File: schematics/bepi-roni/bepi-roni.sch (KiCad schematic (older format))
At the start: 45 parts, among them J1 Conn_01x02, J2 Conn_01x04, J3 Conn_01x25, J4 Conn_01x24, SW1 SW_Push, U1 65C02, U10 SD_SLOT, U2 LM555, U3 AT28C64B, U4 22V10C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

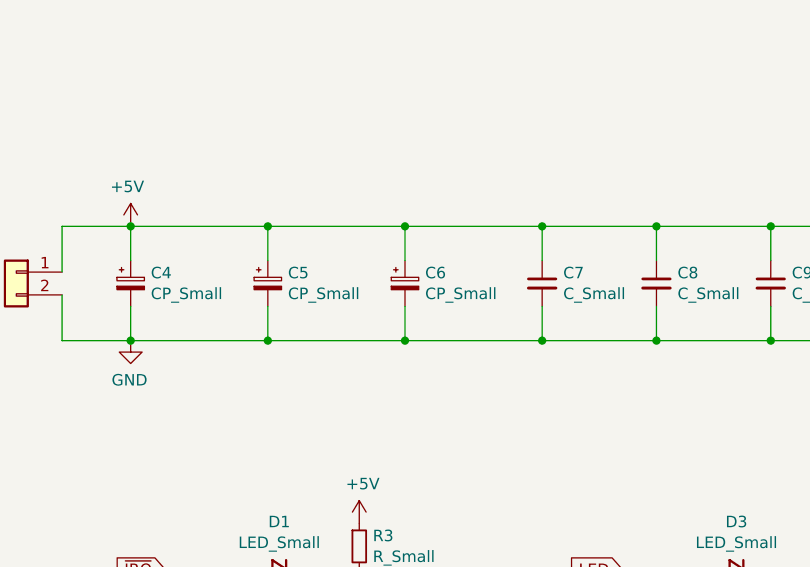
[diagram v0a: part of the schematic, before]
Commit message: added footprints
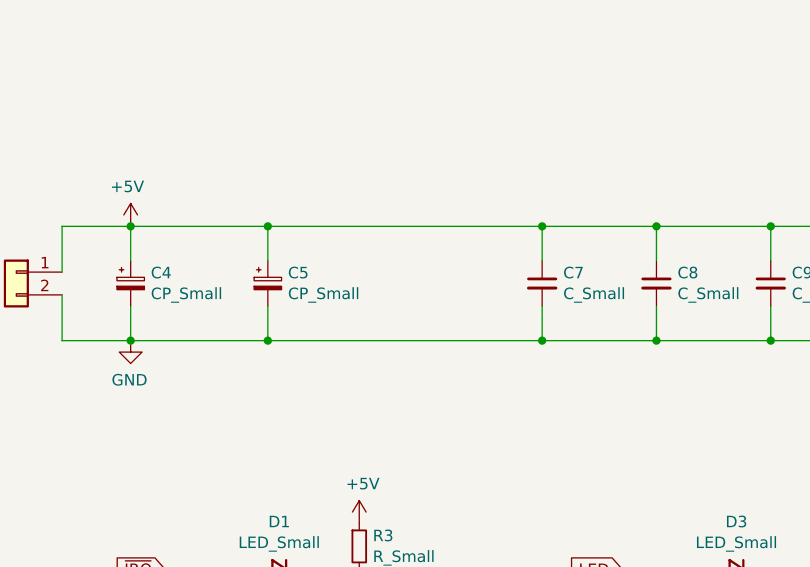
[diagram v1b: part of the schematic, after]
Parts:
- removed C6: CP_Small, symbol Device:CP_Small
- C1, C10, C11, C12, C13, C14, C15, C16, C17, C2, C7, C8, C9: footprint (none) -> Capacitor_THT:C_Disc_D5.0mm_W2.5mm_P5.00mm
- C18, C4, C5: footprint (none) -> Capacitor_THT:CP_Radial_D5.0mm_P2.50mm
- C3: footprint (none) -> Capacitor_THT:CP_Radial_D6.3mm_P2.50mm
- D1, D2, D3, D4: footprint (none) -> LED_THT:LED_D5.0mm
- J1: footprint (none) -> Connector_PinHeader_2.54mm:PinHeader_1x01_P2.54mm_Vertical
- J2: footprint (none) -> Connector_PinHeader_2.54mm:PinHeader_1x04_P2.54mm_Vertical
- J3: footprint (none) -> Connector_PinHeader_2.54mm:PinHeader_1x25_P2.54mm_Vertical
- J4: footprint (none) -> Connector_PinHeader_2.54mm:PinHeader_1x24_P2.54mm_Vertical
- R1, R2, R3, R4, R5, R6: footprint (none) -> Resistor_THT:R_Axial_DIN0207_L6.3mm_D2.5mm_P10.16mm_Horizontal
- RV1: footprint (none) -> Potentiometer_THT:Potentiometer_Bourns_PTV09A-1_Single_Vertical
- SW1: footprint (none) -> Button_Switch_THT:SW_Tactile_Straight_KSA0Axx1LFTR
- U1, U6, U8: footprint (none) -> Package_DIP:DIP-40_W15.24mm
- U10: footprint (none) -> Connector_PinHeader_2.54mm:PinHeader_1x06_P2.54mm_Vertical
- U2: footprint (none) -> Package_DIP:DIP-8_W7.62mm
- U3: footprint (none) -> Package_DIP:DIP-28_W15.24mm
- U4: footprint (none) -> Package_DIP:DIP-24_W7.62mm
- U5: footprint (none) -> Package_DIP:DIP-32_W15.24mm
- U7: footprint (none) -> Connector_PinHeader_2.54mm:PinHeader_1x16_P2.54mm_Vertical
- U9: footprint Package_TO_SOT_SMD:SOT-223-3_TabPin2 -> Package_TO_SOT_THT:TO-220-3_Vertical
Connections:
- wire segments 381 -> 377
